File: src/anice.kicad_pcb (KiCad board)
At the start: 4 copper layers, 65.6 x 34 mm, 94 parts, among them J1 Conn_02x20_Counter_Clockwise, J2 Micro_SD_Card_Det1, J3 USB_C_Receptacle_USB2.0_14P, J4 USB_C_Receptacle_USB2.0_14P, J5 USB_C_Receptacle_USB2.0_14P, J7 HDMI_C_1.3, U1 ECP5U_12_CABGA256, U10 W9825G6KH-6, U11 W25Q128JVS, U12 TLV62569DRL, U13 TLV62569DRL, U14 TLV62569DRL, U5 TPD2EUSB30, U6 TPD2EUSB30, U7 FT231XQ, U8 TPD2EUSB30, U9 PCA9306DC1, Y1 ECS-2520MV-xxx-xx

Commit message: Structure project
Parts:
- added C43: 100nF, Capacitor_SMD:C_0402_1005Metric, B.Cu at (135.8, 87.1)
- moved C38 0.59 mm to (136.7, 88.4)
- moved C36 0.30 mm to (137.6, 90.8)
- moved C2 0.29 mm to (136.1, 84.6)
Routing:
- net +3V3: track 76.1 -> 77.9 mm, vias 34 -> 44
- net +5V: track 176.1 -> 177.5 mm
- net +1V1: track 52.6 -> 53.5 mm
- net GND: vias 60 -> 54

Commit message: Clean up repo
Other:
- board text added: "Change files on the right side!!! -> These two pcbs will be joined together physically"
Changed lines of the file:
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@@
 		(layer "Edge.Cuts")
+	)
+	(gr_text "Change files on the right side!!! ->\nThese two pcbs will be joined together physically"
+		(at 164.36 33.03 0)
+		(layer "Cmts.User")
+		(effects
+			(font
+				(size 3 3)
+				(thickness 0.6)
+				(bold yes)
+			)
+			(justify left bottom)
+		)
 	)
 	(segment

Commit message: Rev 2
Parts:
- added D2: GREEN, LED_SMD:LED_0603_1608Metric, F.Cu at (162.8, 96.5)
- added D3: YELLOW, LED_SMD:LED_0603_1608Metric, F.Cu at (162.8, 98.0)
- added JP1: Jumper_3_Bridged12, Jumper:SolderJumper-3_P1.3mm_Bridged2Bar12_RoundedPad1.0x1.5mm, B.Cu at (122.5, 101.5)
- added R25: 549, Resistor_SMD:R_0603_1608Metric, F.Cu at (165.8, 96.5)
- added R26: 549, Resistor_SMD:R_0603_1608Metric, F.Cu at (165.8, 98.0)
- C13, C14, C15, C16, C17, C18, C19, C20: footprint Capacitor_SMD:C_0603_1608Metric -> Capacitor_SMD:C_0402_1005Metric
- C40: value 15pF -> 5pF
- moved R8 1.96 mm to (111.3, 94.8)
- moved R10 1.96 mm to (108.4, 94.8)
- moved R9 1.96 mm to (109.8, 94.8)
- moved C20 1.86 mm to (112.5, 95.5)
- moved C19 1.40 mm to (113.4, 95.5)
- moved C18 1.00 mm to (114.3, 95.5)
- moved C15 0.98 mm to (117.2, 95.5)
- moved C17 0.77 mm to (115.3, 95.5)
- moved R1 0.74 mm to (129.6, 98.5)
- moved C16 0.55 mm to (116.2, 95.5)
- moved J2 0.18 mm to (109.2, 84.8)
- moved C26 0.11 mm to (133.2, 86.4)
- moved C43 0.08 mm to (135.8, 87.2)
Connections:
- U1 pad C13: unconnected-(U1C-PT60B/--PadC13) -> LED1
- U1 pad D14: unconnected-(U1D-PR2D/-/RDQ8-PadD14) -> LED2
- U7 pad 11: FT2V5 -> Net-(JP1-C)
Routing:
- net LED1: track 0.00 -> 31.3 mm, vias 0 -> 2
- net LED2: track 0.00 -> 30.2 mm, vias 0 -> 2
- net +1V1: track 53.5 -> 31.4 mm, vias 10 -> 12
- net GND: track 94.4 -> 115.7 mm, vias 54 -> 68
- net +5V: track 177.5 -> 195.8 mm, vias 14 -> 13
- net +3V3: track 77.9 -> 89.3 mm, vias 44 -> 41
- net Net-(JP1-C): track 0.00 -> 3.67 mm, vias 0 -> 1
- net Net-(J7-UTILITY): track 5.06 -> 3.11 mm
- net Net-(J7-HPD): track 5.23 -> 3.28 mm
- net FT2V5: track 21.2 -> 23.1 mm
- net FPDI_UTIL: track 26.3 -> 24.4 mm
- net FPDI_CEC: track 22.8 -> 20.9 mm
- net Net-(J7-CK-): track 4.13 -> 2.27 mm
- net FPDI_HPD: track 29.6 -> 27.7 mm
- net Net-(J7-CEC): track 4.80 -> 3.25 mm
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- added copper zone on In2.Cu, net +1V1

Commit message: Tidy project
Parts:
- moved C14 1.32 mm to (119.0, 95.7)
- moved C13 1.32 mm to (119.0, 96.7)
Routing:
- net FPDI_D2+: track 14.9 -> 16.4 mm
- net FPDI_D2-: track 14.9 -> 16.4 mm
- net Net-(J7-D2-): track 4.06 -> 2.85 mm
- net Net-(J7-D2+): track 2.88 -> 2.01 mm
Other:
- board text added: "Change files on the right side!!! -> These two pcbs will be joined together physically Scroll to zoom, Right click & drag to pan"
- board text removed: "Change files on the right side!!! -> These two pcbs will be joined together physically"

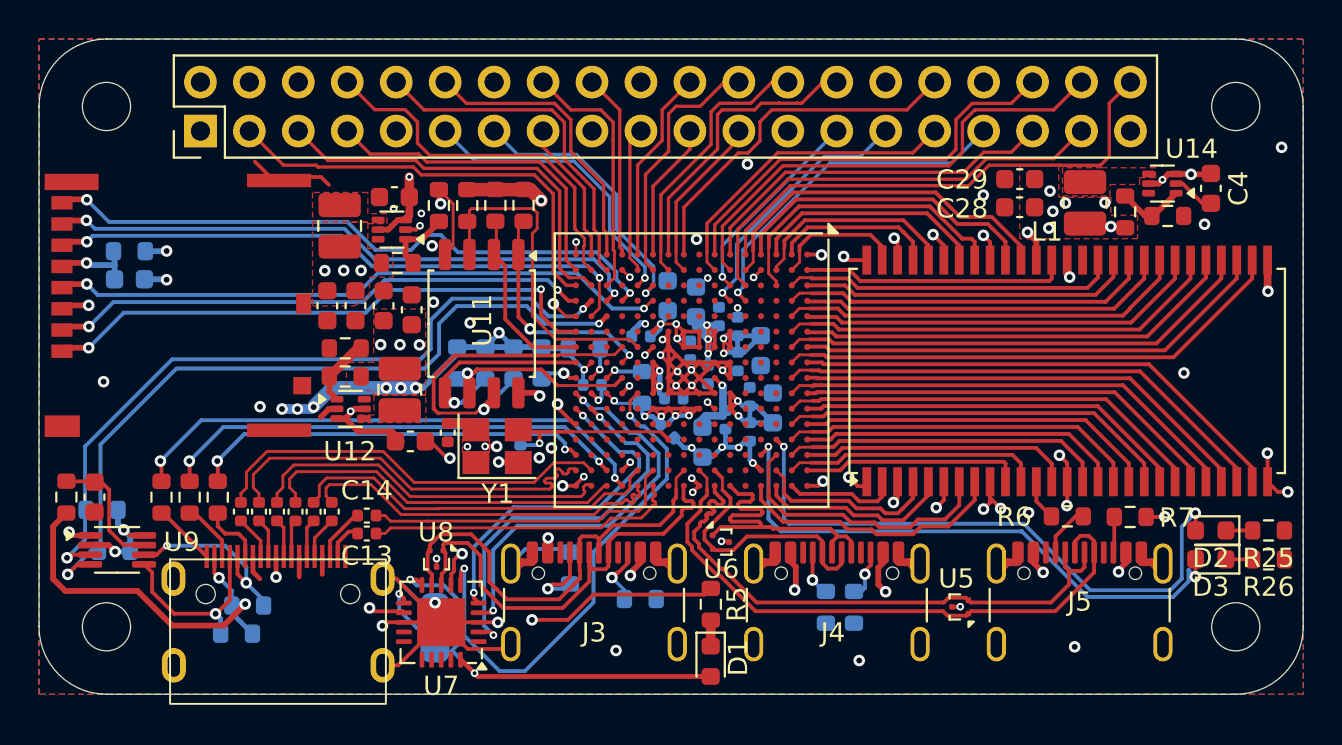
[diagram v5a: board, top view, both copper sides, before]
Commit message: Add test points
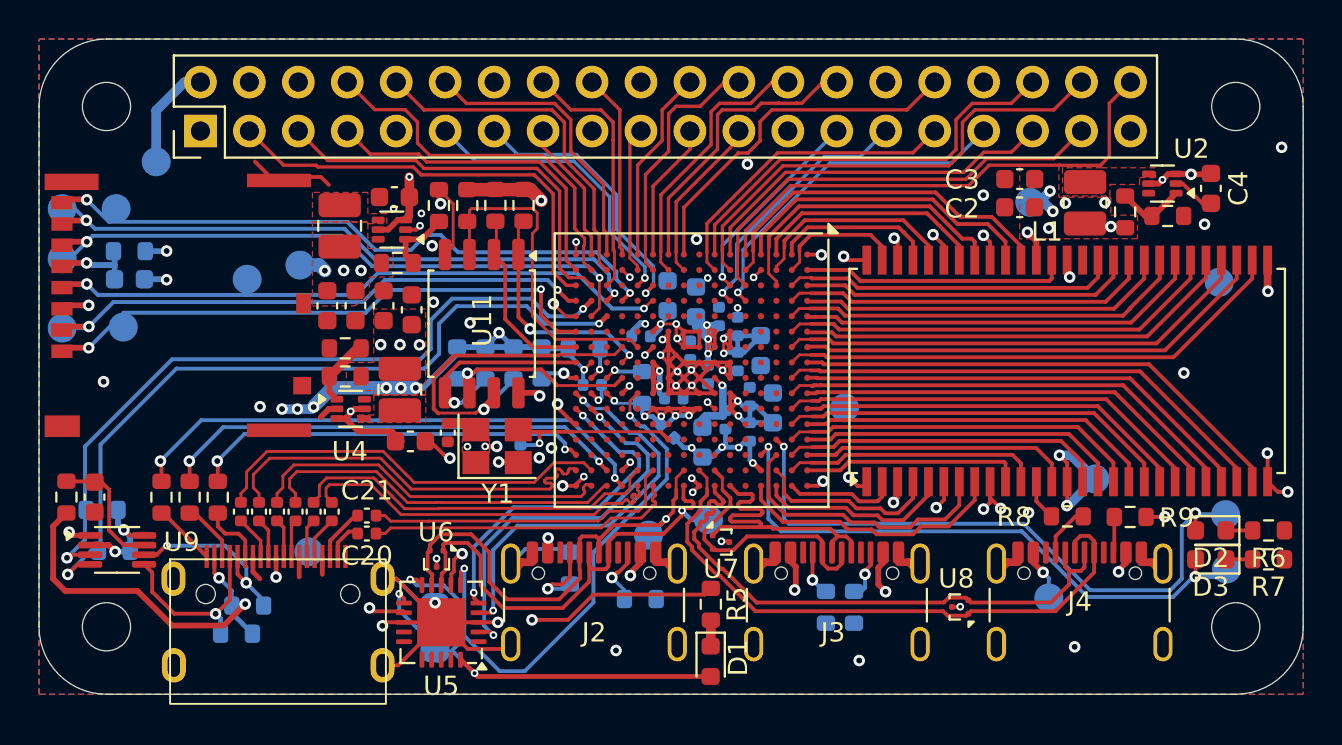
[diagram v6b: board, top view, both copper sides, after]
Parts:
- added 1V1: TestPoint, TestPoint:TestPoint_Pad_D1.5mm, B.Cu at (153.4, 79.5)
- added 2V1: TestPoint, TestPoint:TestPoint_Pad_D1.5mm, B.Cu at (115.5, 82.7)
- added 3V1: TestPoint, TestPoint:TestPoint_Pad_D1.5mm, B.Cu at (156.8, 93.8)
- added 5V1: TestPoint, TestPoint:TestPoint_Pad_D1.5mm, B.Cu at (108.1, 77.4)
- added 5V2: TestPoint, TestPoint:TestPoint_Pad_D1.5mm, B.Cu at (154.4, 100.0)
- added CLK1: TestPoint, TestPoint:TestPoint_Pad_D1.5mm, B.Cu at (112.8, 83.5)
- added CMD1: TestPoint, TestPoint:TestPoint_Pad_D1.5mm, B.Cu at (103.2, 82.4)
- added DM1: TestPoint, TestPoint:TestPoint_Pad_D1.5mm, B.Cu at (133.6, 96.7)
- added DP1: TestPoint, TestPoint:TestPoint_Pad_D1.5mm, B.Cu at (136.7, 95.9)
- added GND1: TestPoint, TestPoint:TestPoint_Pad_D1.5mm, B.Cu at (163.2, 83.6)
- added GND2: TestPoint, TestPoint:TestPoint_Pad_D1.5mm, B.Cu at (116.0, 97.6)
- added GND3: TestPoint, TestPoint:TestPoint_Pad_D1.5mm, B.Cu at (143.8, 90.1)
- added LED1: TestPoint, TestPoint:TestPoint_Pad_D1.5mm, B.Cu at (163.6, 95.7)
- added LED2: TestPoint, TestPoint:TestPoint_Pad_D1.5mm, B.Cu at (163.6, 98.5)
- added SD0: TestPoint, TestPoint:TestPoint_Pad_D1.5mm, B.Cu at (103.2, 86.0)
- added SD1: TestPoint, TestPoint:TestPoint_Pad_D1.5mm, B.Cu at (106.4, 86.0)
- added SD2: TestPoint, TestPoint:TestPoint_Pad_D1.5mm, B.Cu at (106.0, 79.8)
- added SD3: TestPoint, TestPoint:TestPoint_Pad_D1.5mm, B.Cu at (103.2, 79.8)
- renumbered C43 to C1, C42 to C10, C27 to C12, C8 to C13, C9 to C14, C10 to C15, C12 to C16, C23 to C17, C39 to C18, C40 to C19, C28 to C2, C13 to C20, C14 to C21, C15 to C22, C16 to C23, C17 to C24, C18 to C25, C19 to C26, C20 to C27, C21 to C28, C30 to C29, C29 to C3, C31 to C30, C32 to C31, C33 to C32, C34 to C33, C35 to C34, C25 to C35, C26 to C36, C41 to C37, C22 to C38, C3 to C5, C2 to C6, C38 to C7, C36 to C8, C37 to C9, J3 to J2, J4 to J3, J5 to J4, J7 to J5, J2 to J6, R11 to R10, R12 to R11, R13 to R12, R14 to R13, R15 to R14, R8 to R15, R9 to R16, R10 to R17, R16 to R18, R17 to R19, R18 to R20, R19 to R21, R20 to R22, R21 to R23, R22 to R24, R23 to R25, R24 to R26, R38 to R27, R25 to R6, R26 to R7, R6 to R8, R7 to R9, U14 to U2, U13 to U3, U12 to U4, U7 to U5, U8 to U6, U6 to U7, U5 to U8
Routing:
- net +5V: track 195.8 -> 202.8 mm
- net +3V3: track 89.3 -> 93.6 mm
- net +1V1: track 31.4 -> 34.1 mm
- net +2V5: track 25.2 -> 26.9 mm
- net SD_CMD: track 31.1 -> 32.7 mm
- net LED1: track 31.3 -> 32.9 mm
- net D1+: track 23.2 -> 24.7 mm, vias 0 -> 1
- net SD_D0: track 28.1 -> 29.7 mm
- net SD_D3: track 31.3 -> 32.8 mm
- net D1-: track 24.0 -> 25.3 mm, vias 0 -> 1
- net LED2: track 30.2 -> 31.3 mm
- net SD_CLK: track 32.3 -> 33.1 mm
